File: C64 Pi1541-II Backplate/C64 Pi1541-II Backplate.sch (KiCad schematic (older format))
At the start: 4 parts, among them M1 Mounting, M2 Mounting, M3 Mounting, M4 Mounting

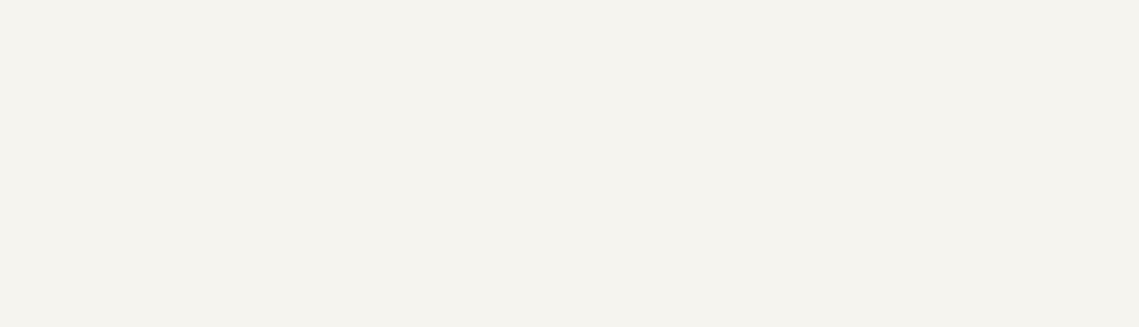
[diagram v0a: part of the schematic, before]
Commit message: Added DIN cutout
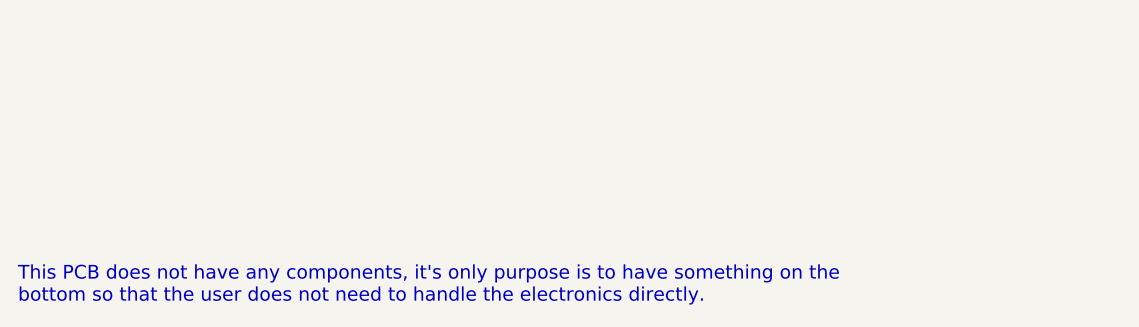
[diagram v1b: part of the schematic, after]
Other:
- note added: "This PCB does not have any components, it's only purpose is to have something on the\nbottom so that the user does not need to handle the electronics directly."
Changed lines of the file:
@@
 	1    0    0    -1
 $EndComp
+Text Notes 7000 6750 0    60   ~ 0
+This PCB does not have any components, it's only purpose is to have something on the\nbottom so that the user does not need to handle the electronics directly.
 $EndSCHEMATC

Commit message: Added copper layer to backplate
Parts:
- M1, M2, M3, M4: footprint mounting:M3 -> mounting:M3_pin; symbol mounting:Mounting -> Connector:Conn_01x01_Female
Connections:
- new net: M1.1 (Pin_1), M2.1 (Pin_1), M3.1 (Pin_1), M4.1 (Pin_1)
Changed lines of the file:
@@
 $EndDescr
 $Comp
-L mounting:Mounting M1
+L Connector:Conn_01x01_Female M1
 U 1 1 5E3B603D
 P 10650 625
 F 0 "M1" H 10650 725 50  0001 C CNN
 F 1 "Mounting" H 10650 550 50  0001 C CNN
-F 2 "mounting:M3" H 10650 625 50  0001 C CNN
+F 2 "mounting:M3_pin" H 10650 625 50  0001 C CNN
 F 3 "" H 10650 625 50  0001 C CNN
 	1    10650 625
-	1    0    0    -1
+	0    -1   -1   0
 $EndComp
 $Comp
-L mounting:Mounting M2
+L Connector:Conn_01x01_Female M2
 U 1 1 5E3B604F
 P 10775 625
 F 0 "M2" H 10775 725 50  0001 C CNN
 F 1 "Mounting" H 10775 550 50  0001 C CNN
-F 2 "mounting:M3" H 10775 625 50  0001 C CNN
+F 2 "mounting:M3_pin" H 10775 625 50  0001 C CNN
 F 3 "" H 10775 625 50  0001 C CNN
 	1    10775 625
-	1    0    0    -1
+	0    -1   -1   0
 $EndComp
 $Comp
-L mounting:Mounting M3
+L Connector:Conn_01x01_Female M3
 U 1 1 5E3B605A
 P 10900 625
 F 0 "M3" H 10900 725 50  0001 C CNN
 F 1 "Mounting" H 10900 550 50  0001 C CNN
-F 2 "mounting:M3" H 10900 625 50  0001 C CNN
+F 2 "mounting:M3_pin" H 10900 625 50  0001 C CNN
 F 3 "" H 10900 625 50  0001 C CNN
 	1    10900 625
-	1    0    0    -1
+	0    -1   -1   0
 $EndComp
 $Comp
-L mounting:Mounting M4
+L Connector:Conn_01x01_Female M4
 U 1 1 5E3B6065
 P 11025 625
 F 0 "M4" H 11025 725 50  0001 C CNN
 F 1 "Mounting" H 11025 550 50  0001 C CNN
-F 2 "mounting:M3" H 11025 625 50  0001 C CNN
+F 2 "mounting:M3_pin" H 11025 625 50  0001 C CNN
 F 3 "" H 11025 625 50  0001 C CNN
 	1    11025 625
-	1    0    0    -1
+	0    -1   -1   0
 $EndComp
 Text Notes 7000 6750 0    60   ~ 0
 This PCB does not have any components, it's only purpose is to have something on the\nbottom so that the user does not need to handle the electronics directly.
+Wire Wire Line
+	10650 825  10650 900
+Wire Wire Line
+	10650 900  10775 900
+Wire Wire Line
+	11025 900  11025 825
+Wire Wire Line
+	10775 825  10775 900
+Connection ~ 10775 900
+Wire Wire Line
+	10775 900  10900 900
+Wire Wire Line
+	10900 825  10900 900
+Connection ~ 10900 900
+Wire Wire Line
+	10900 900  11025 900
 $EndSCHEMATC
